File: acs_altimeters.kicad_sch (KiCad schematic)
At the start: 15 parts, among them U4 BMP581, U5 BMP581, U6 BMP581

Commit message: Fixed symbols and ran ERC
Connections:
- net INT_A1: now reaches U5.7 (INT)
- net INT_A2: now reaches U6.7 (INT)
- net INT_A0: now reaches U4.7 (INT)
- net 3.3V renamed +3.3V
- net CS4 renamed CS_A0
- net CS5 renamed CS_A1
- net CS6 renamed CS_A2
- net SCK renamed SCK0
- net SCK0: no longer U5.2 (SCK)
- net SDI renamed MOSI0
- net MOSI0: no longer U5.4 (SDI)
- net SDO renamed MISO0
- net MISO0: no longer U5.5 (SDO)
- new net MISO1: U5.5 (SDO)
- new net MOSI1: U5.4 (SDI)
- new net SCK1: U5.2 (SCK)
- no-connect marks 3 -> 0
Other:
- note added: "Altimeter"
- note added: "Altimeter 1"
- note added: "Altimeter 2"
- note added: "Altimeter 3"
- note removed: "interrupts?"

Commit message: miso-mosi-fix
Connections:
- net GND: no longer C10.1, C11.2, C12.1, C7.2, C8.2, C9.1, U4.3 (VSS), U5.3 (VSS), U6.3 (VSS)
- new net: C7.2, C9.1, U4.3 (VSS)
- new net: C10.1, C8.2, U5.3 (VSS)
- new net: C11.2, C12.1, U6.3 (VSS)
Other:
- moved on the sheet: C10, C11, C12, C7, C8, C9, R3, R4, R5, R6, R7, R8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

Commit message: created PCB and layout
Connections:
- net GND: now also C10.1, C11.2, C12.1, C7.2, C8.2, C9.1, U4.3 (VSS), U5.3 (VSS), U6.3 (VSS)

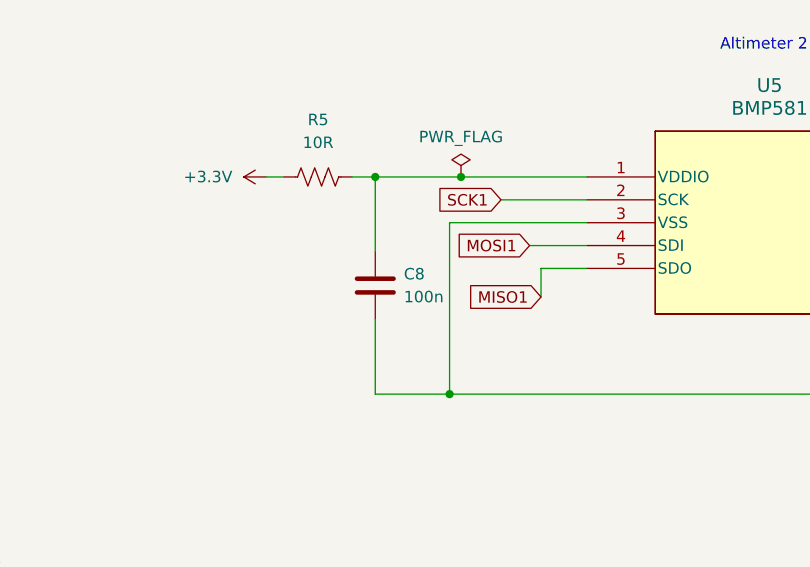
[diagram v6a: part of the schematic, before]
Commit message: Redid Footprints/Picked components
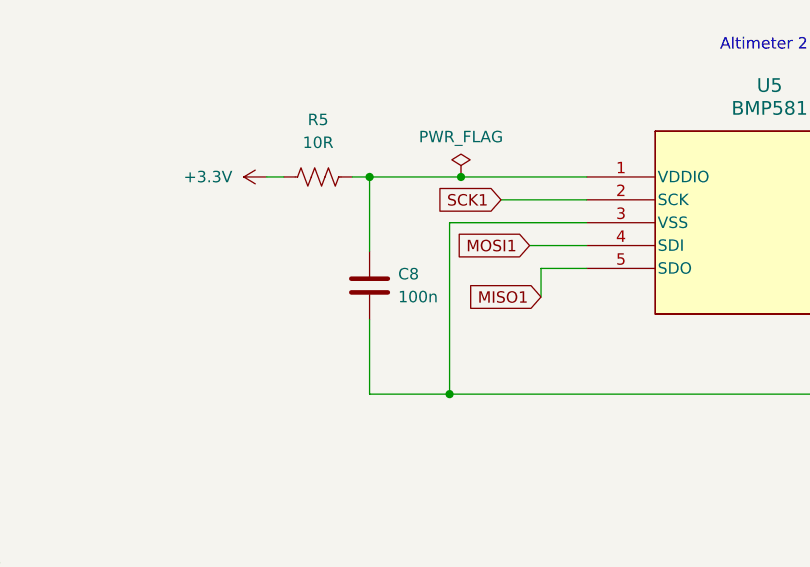
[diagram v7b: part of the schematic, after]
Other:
- moved on the sheet: C8
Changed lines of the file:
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@@
-	)
-	(junction
-		(at 178.435 87.63)
-		(diameter 0)
-		(color 0 0 0 0)
 	)
 	(junction
@@
 	)
 	(junction
+		(at 177.8 87.63)
+		(diameter 0)
+		(color 0 0 0 0)
+	)
+	(junction
 		(at 125.73 158.75)
 		(diameter 0)
@@
 	(wire
 		(pts
-			(xy 178.435 111.76) (xy 186.69 111.76)
+			(xy 177.8 111.76) (xy 186.69 111.76)
 		)
 		(stroke
@@
 	(wire
 		(pts
-			(xy 178.435 87.63) (xy 187.96 87.63)
-		)
-		(stroke
-			(width 0)
-			(type default)
-		)
-	)
-	(wire
-		(pts
 			(xy 139.065 134.62) (xy 140.335 134.62)
 		)
@@
 	(wire
 		(pts
+			(xy 177.8 87.63) (xy 187.96 87.63)
+		)
+		(stroke
+			(width 0)
+			(type default)
+		)
+	)
+	(wire
+		(pts
 			(xy 113.03 134.62) (xy 118.11 134.62)
 		)
@@
 	(wire
 		(pts
-			(xy 178.435 95.885) (xy 178.435 87.63)
+			(xy 177.8 95.885) (xy 177.8 87.63)
 		)
 		(stroke
@@
 	(wire
 		(pts
-			(xy 175.895 87.63) (xy 178.435 87.63)
+			(xy 175.895 87.63) (xy 177.8 87.63)
 		)
 		(stroke
@@
 	(wire
 		(pts
-			(xy 178.435 103.505) (xy 178.435 111.76)
+			(xy 177.8 103.505) (xy 177.8 111.76)
 		)
 		(stroke
@@
 	(symbol
 		(lib_id "Device:C")
-		(at 178.435 99.695 0)
+		(at 177.8 99.695 0)
 		(unit 1)
 		(body_style 1)
@@
 		(fields_autoplaced yes)
 		(property "Reference" "C8"
-			(at 181.61 98.4249 0)
+			(at 180.975 98.4249 0)
 			(show_name no)
 			(do_not_autoplace no)
@@
 		)
 		(property "Value" "100n"
-			(at 181.61 100.9649 0)
+			(at 180.975 100.9649 0)
 			(show_name no)
 			(do_not_autoplace no)
@@
 		)
 		(property "Footprint" "Capacitor_SMD:C_0603_1608Metric"
-			(at 179.4002 103.505 0)
+			(at 178.7652 103.505 0)
 			(hide yes)
 			(show_name no)
@@
 		)
 		(property "Datasheet" ""
-			(at 178.435 99.695 0)
+			(at 177.8 99.695 0)
 			(hide yes)
 			(show_name no)
@@
 		)
 		(property "Description" "Unpolarized capacitor"
-			(at 178.435 99.695 0)
-			(hide yes)
-			(show_name no)
+			(at 177.8 99.695 0)
+			(hide yes)
+			(show_name no)
